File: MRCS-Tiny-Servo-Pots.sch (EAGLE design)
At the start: 11 parts, among them CON1 CONNECTOR-M03254-LOCK, U1 ATTINY85-20SH

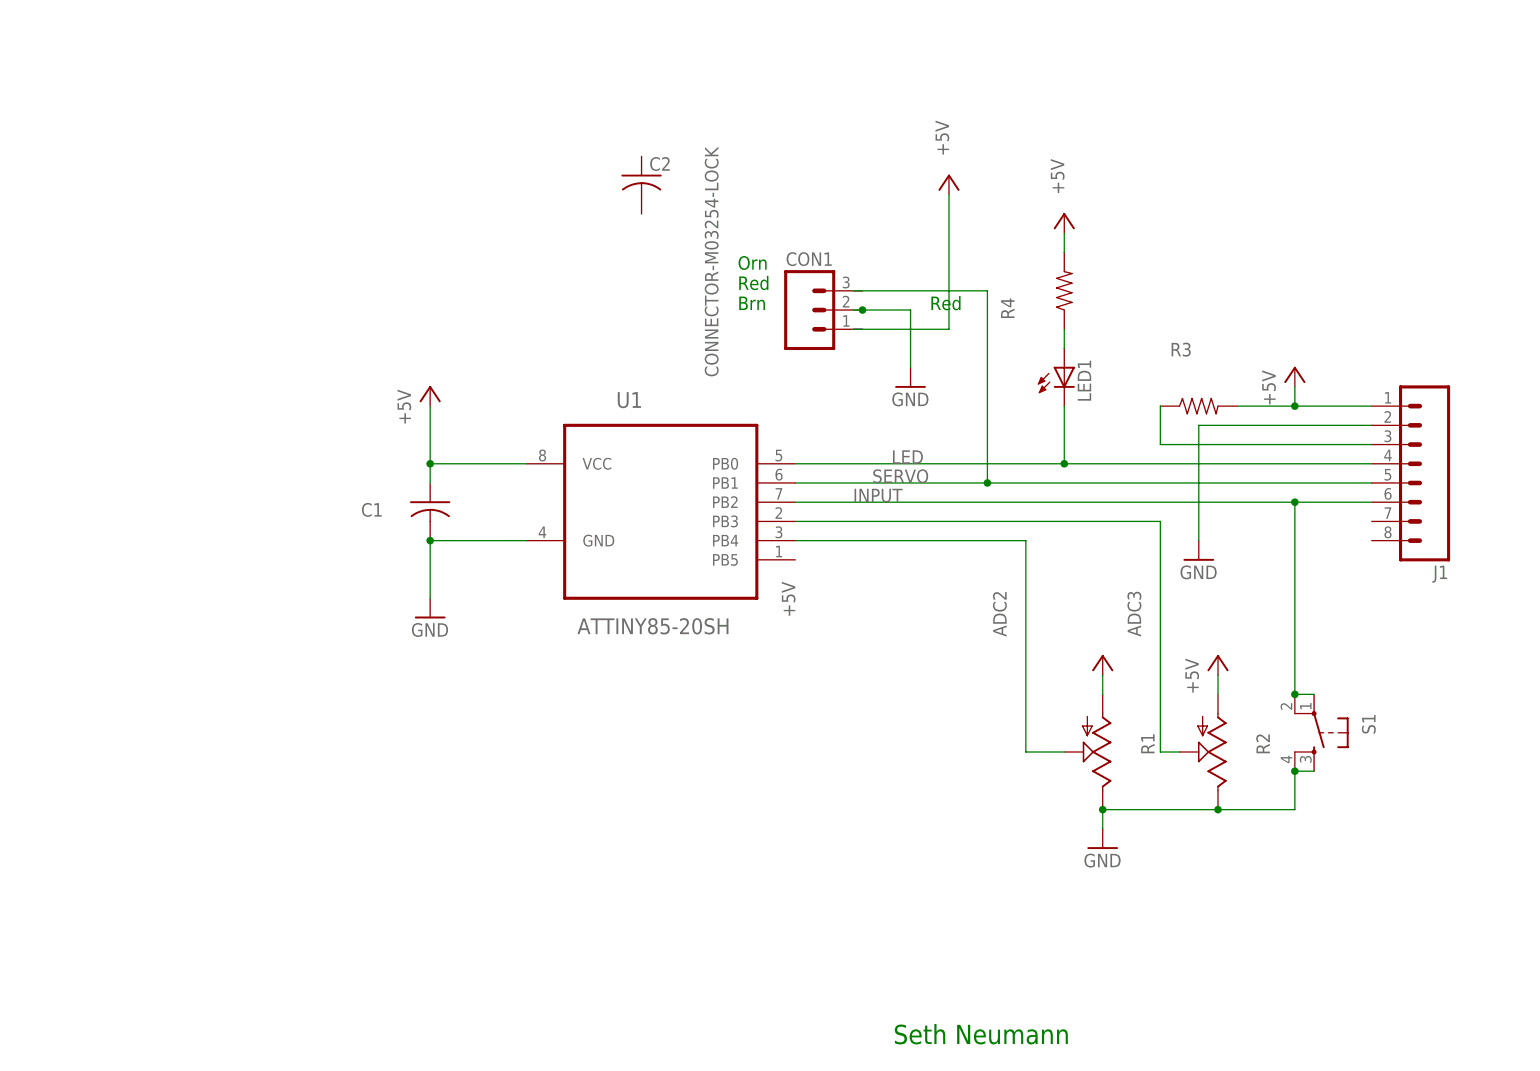
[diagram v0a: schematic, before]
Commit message: first pass to production
this one is a little too big to go 2x3 so some changes will be made, also considering going surface mount, but only 2 resistors and a LED, the rest would be thru hole
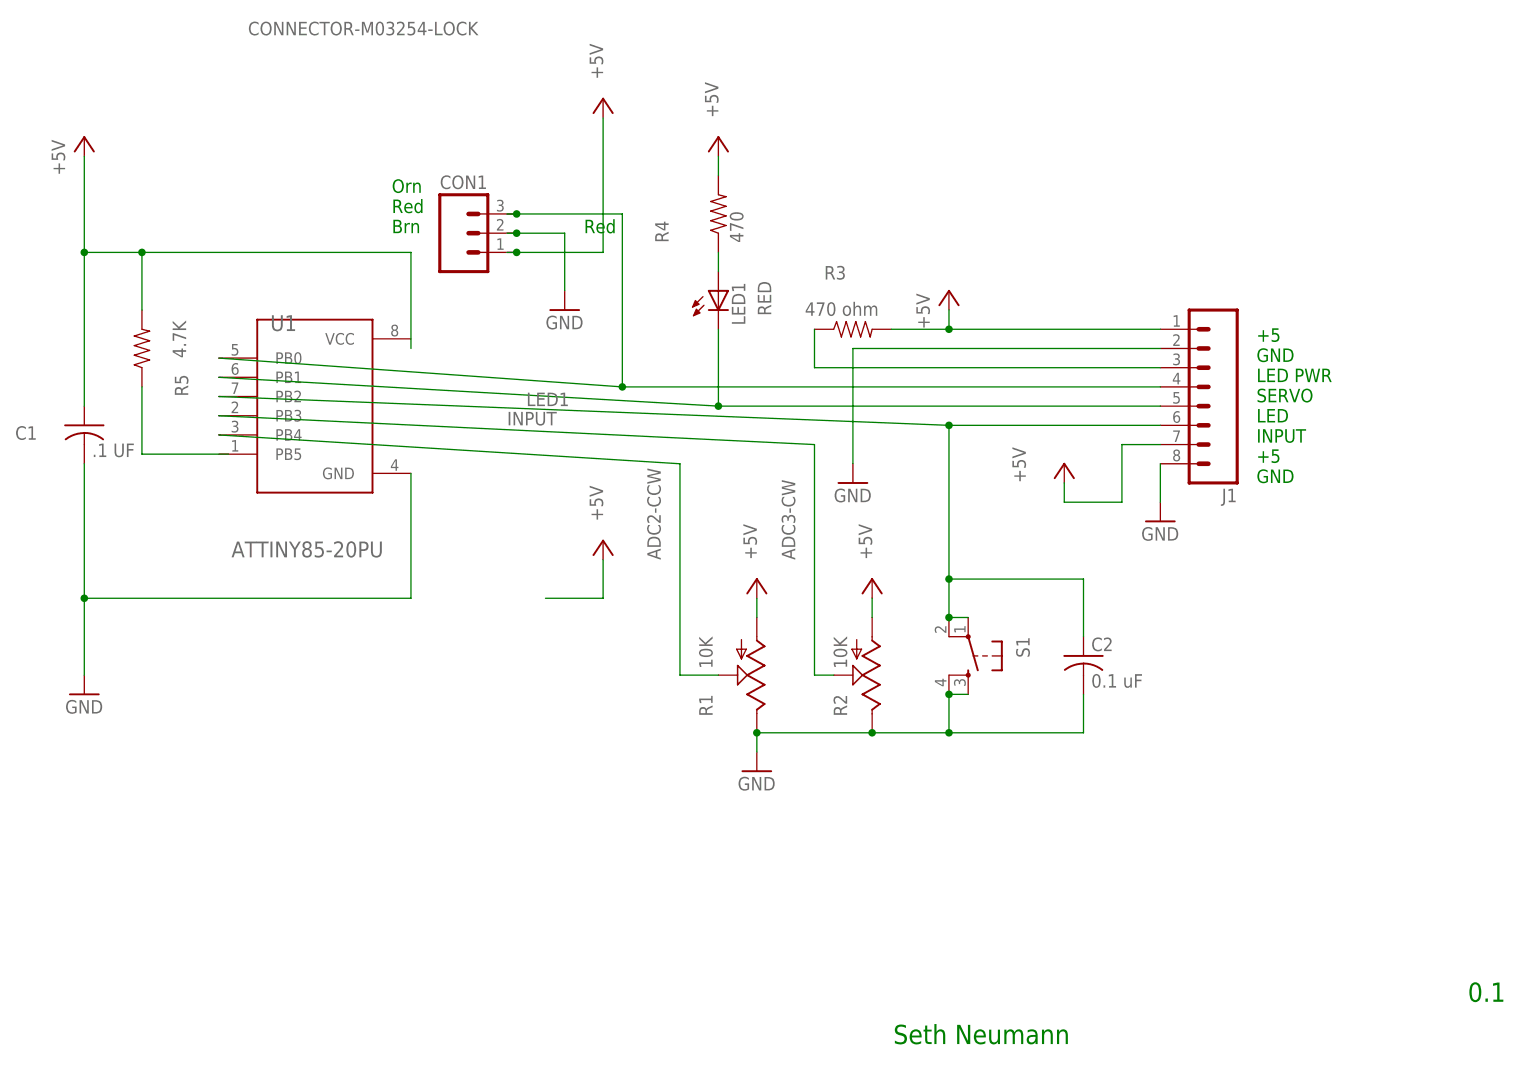
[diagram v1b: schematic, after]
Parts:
- added R5: 4.7K, SPCoast:RPTH04
- C1: value (none) -> .1 UF
- C2: value (none) -> 0.1 uF
- LED1: value (none) -> RED
- R1, R2: value (none) -> 10K
- R3: value (none) -> 470 ohm
- R4: value (none) -> 470
- U1: value ATTINY85-20SH -> ATTINY85-20PU; device ATTINY85-20SH:ATTINY85-20SH -> ATTINY85-20PU:ATTINY85-20PU
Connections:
- net ADC2 renamed ADC2-CCW
- net ADC3 renamed ADC3-CW
- removed net LED: J1.4, LED1.C, U1.PB0
- removed net SERVO: J1.5, U1.PB1
- new net LED1: J1.5, LED1.C, U1.PB1
- new net N$3: R5.1
- new net N$4: CON1.3, J1.4, U1.PB0
- net +5V: now also CON1.1, J1.7, R5.2; no longer U1.VCC
- net GND: now also C2.2, J1.8
- net INPUT: now also C2.1
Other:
- note added: "+5 GND LED PWR SERVO LED INPUT +5 GND"
- note added: "0.1"
- moved on the sheet: C1, C2, CON1, J1, LED1, R1, R2, R3, R4, S1, U1
